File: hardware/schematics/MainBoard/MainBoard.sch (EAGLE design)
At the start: 17 parts

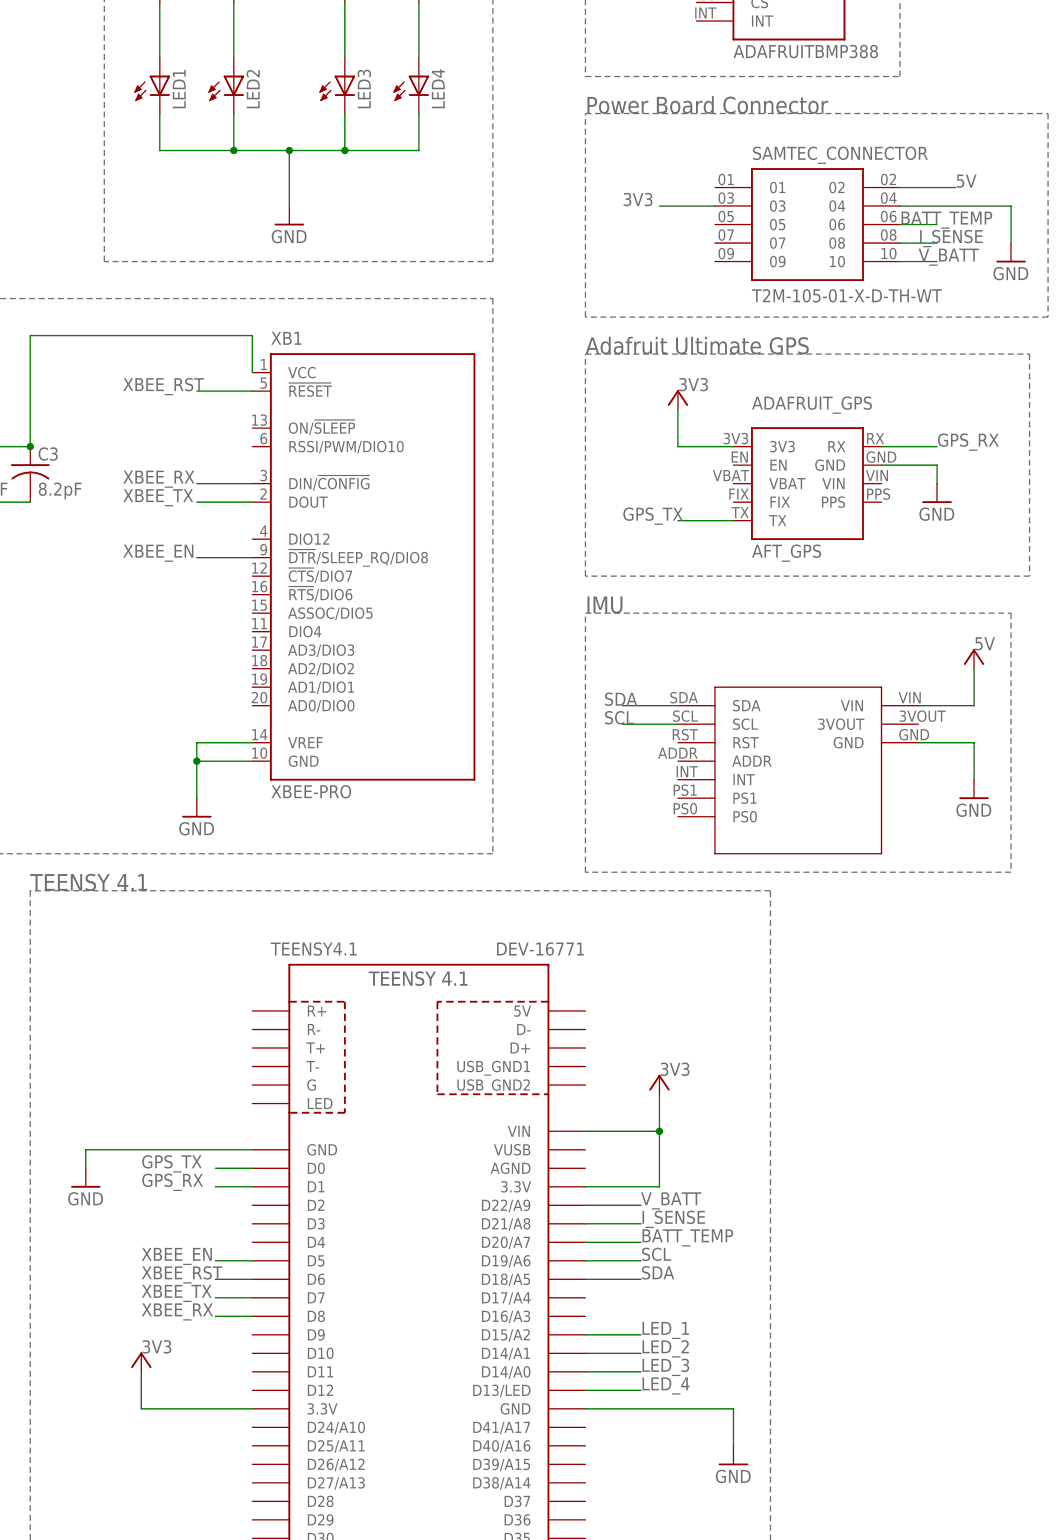
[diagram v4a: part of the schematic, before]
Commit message: MainBoard Power routing & Power Board PNG
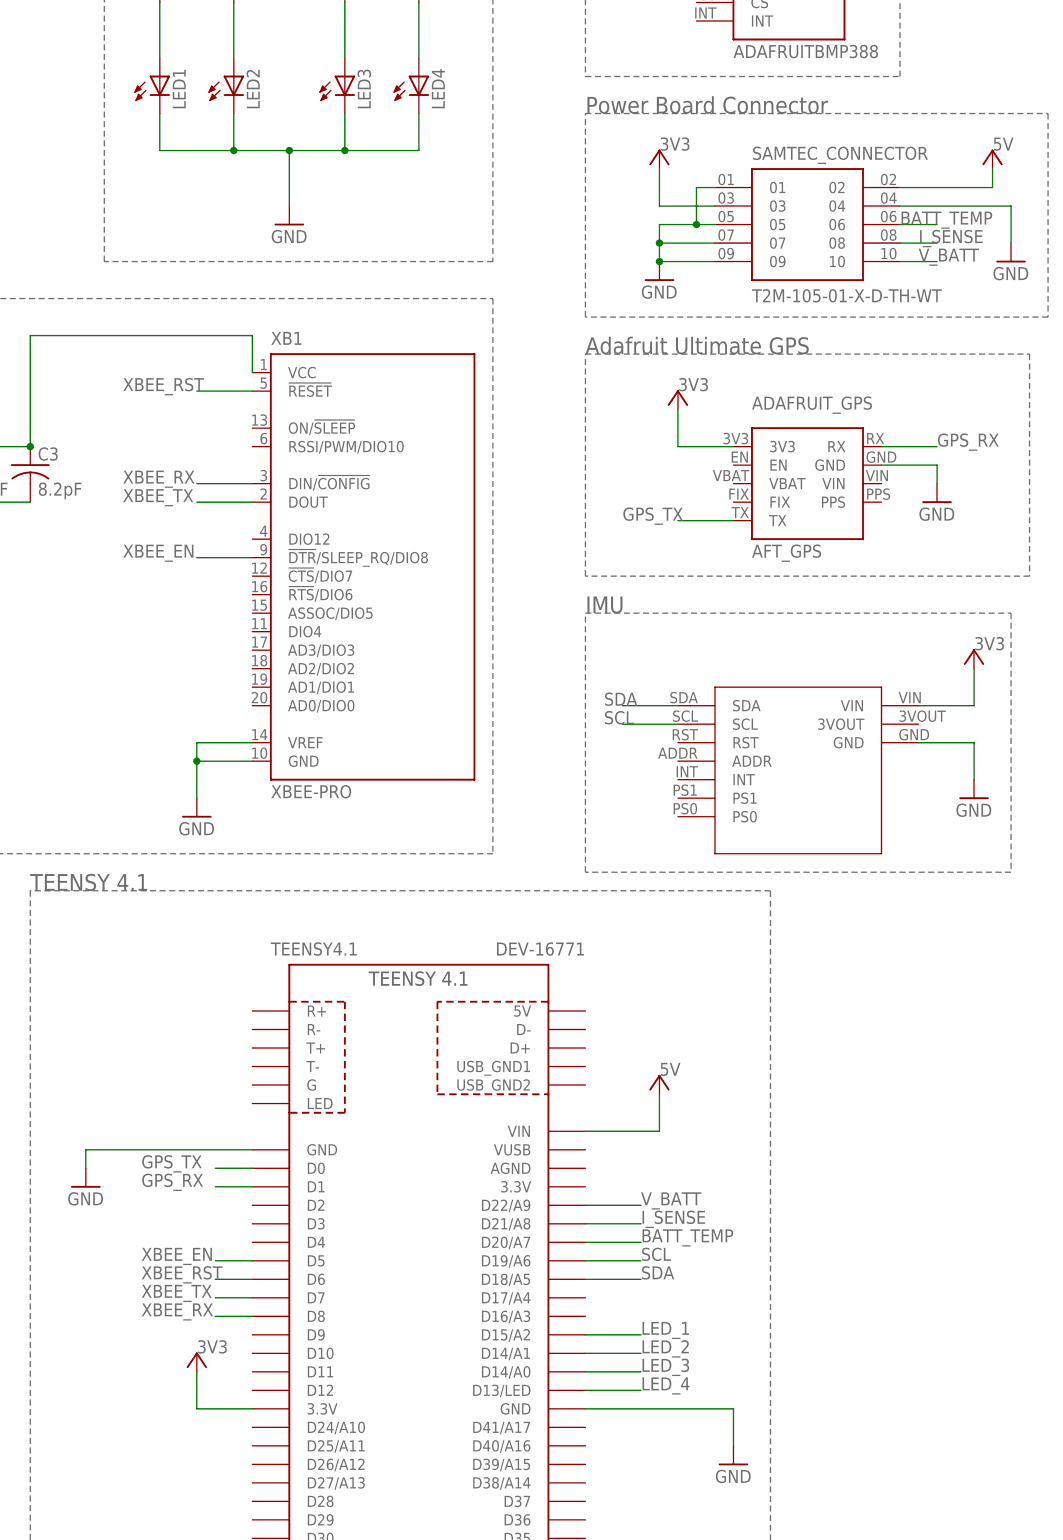
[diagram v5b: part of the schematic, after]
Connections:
- net 3V3: now also U$1.VIN; no longer TEENSY4.1.3.3V@1, TEENSY4.1.VIN
- net 5V: now also TEENSY4.1.VIN; no longer U$1.VIN
- net GND: now also SAMTEC_CONNECTOR.01, SAMTEC_CONNECTOR.05, SAMTEC_CONNECTOR.07, SAMTEC_CONNECTOR.09
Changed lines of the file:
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@@
 <part name="P+4" library="supply1" library_urn="urn:adsk.eagle:library:371" deviceset="VCC" device=""/>
 <part name="GND4" library="supply1" library_urn="urn:adsk.eagle:library:371" deviceset="GND" device=""/>
+<part name="ADAFRUIT_BMP388" library="adafruit BMP388" deviceset="ADAFRUITBMP388" device=""/>
+<part name="GND9" library="supply1" library_urn="urn:adsk.eagle:library:371" deviceset="GND" device=""/>
+<part name="P+6" library="supply1" library_urn="urn:adsk.eagle:library:371" deviceset="VCC" device=""/>
+<part name="P+7" library="supply1" library_urn="urn:adsk.eagle:library:371" deviceset="VCC" device=""/>
 <part name="P+5" library="supply1" library_urn="urn:adsk.eagle:library:371" deviceset="VCC" device=""/>
-<part name="ADAFRUIT_BMP388" library="adafruit BMP388" deviceset="ADAFRUITBMP388" device=""/>
 </parts>
 <sheets>
@@
 <attribute name="VALUE" x="124.46" y="-48.26" size="1.778" layer="96"/>
 </instance>
-<instance part="P+5" gate="VCC" x="12.7" y="-121.92" smashed="yes"/>
 <instance part="ADAFRUIT_BMP388" gate="G$1" x="101.6" y="68.58" smashed="yes">
 <attribute name="VALUE" x="93.98" y="55.88" size="1.778" layer="96"/>
 <attribute name="NAME" x="93.98" y="81.28" size="1.778" layer="95"/>
 </instance>
+<instance part="GND9" gate="1" x="83.82" y="25.4" smashed="yes">
+<attribute name="VALUE" x="81.28" y="22.86" size="1.778" layer="96"/>
+</instance>
+<instance part="P+6" gate="VCC" x="83.82" y="43.18" smashed="yes"/>
+<instance part="P+7" gate="VCC" x="129.54" y="43.18" smashed="yes"/>
+<instance part="P+5" gate="VCC" x="20.32" y="-121.92" smashed="yes"/>
 </instances>
 <busses>
@@
 </segment>
 <segment>
-<pinref part="TEENSY4.1" gate="G$1" pin="VIN"/>
-<wire x1="73.66" y1="-91.44" x2="83.82" y2="-91.44" width="0.1524" layer="91"/>
-<wire x1="83.82" y1="-91.44" x2="83.82" y2="-86.36" width="0.1524" layer="91"/>
-<pinref part="P+3" gate="VCC" pin="VCC"/>
-<label x="83.82" y="-83.82" size="1.778" layer="95"/>
-<pinref part="TEENSY4.1" gate="G$1" pin="3.3V@1"/>
-<wire x1="73.66" y1="-99.06" x2="83.82" y2="-99.06" width="0.1524" layer="91"/>
-<wire x1="83.82" y1="-99.06" x2="83.82" y2="-91.44" width="0.1524" layer="91"/>
-<junction x="83.82" y="-91.44"/>
-</segment>
-<segment>
-<pinref part="SAMTEC_CONNECTOR" gate="G$1" pin="03"/>
-<wire x1="91.44" y1="35.56" x2="83.82" y2="35.56" width="0.1524" layer="91"/>
-<label x="78.74" y="35.56" size="1.778" layer="95"/>
-</segment>
-<segment>
-<pinref part="TEENSY4.1" gate="G$1" pin="3.3V"/>
-<wire x1="27.94" y1="-129.54" x2="12.7" y2="-129.54" width="0.1524" layer="91"/>
-<wire x1="12.7" y1="-129.54" x2="12.7" y2="-124.46" width="0.1524" layer="91"/>
-<pinref part="P+5" gate="VCC" pin="VCC"/>
-<label x="12.7" y="-121.92" size="1.778" layer="95"/>
-</segment>
-<segment>
 <pinref part="ADAFRUIT_BMP388" gate="G$1" pin="VIN"/>
 <wire x1="88.9" y1="78.74" x2="83.82" y2="78.74" width="0.1524" layer="91"/>
 <label x="81.28" y="78.74" size="1.778" layer="95"/>
+</segment>
+<segment>
+<pinref part="SAMTEC_CONNECTOR" gate="G$1" pin="03"/>
+<wire x1="91.44" y1="35.56" x2="83.82" y2="35.56" width="0.1524" layer="91"/>
+<label x="83.82" y="43.18" size="1.778" layer="95"/>
+<pinref part="P+6" gate="VCC" pin="VCC"/>
+<wire x1="83.82" y1="35.56" x2="83.82" y2="40.64" width="0.1524" layer="91"/>
+</segment>
+<segment>
+<pinref part="U$1" gate="G$1" pin="VIN"/>
+<wire x1="119.38" y1="-33.02" x2="127" y2="-33.02" width="0.1524" layer="91"/>
+<wire x1="127" y1="-33.02" x2="127" y2="-27.94" width="0.1524" layer="91"/>
+<pinref part="P+4" gate="VCC" pin="VCC"/>
+<label x="127" y="-25.4" size="1.778" layer="95"/>
+</segment>
+<segment>
+<pinref part="TEENSY4.1" gate="G$1" pin="3.3V"/>
+<wire x1="27.94" y1="-129.54" x2="20.32" y2="-129.54" width="0.1524" layer="91"/>
+<wire x1="20.32" y1="-129.54" x2="20.32" y2="-124.46" width="0.1524" layer="91"/>
+<pinref part="P+5" gate="VCC" pin="VCC"/>
+<label x="20.32" y="-121.92" size="1.778" layer="95"/>
 </segment>
 </net>
@@
 <label x="81.28" y="73.66" size="1.778" layer="95"/>
 </segment>
+<segment>
+<pinref part="SAMTEC_CONNECTOR" gate="G$1" pin="05"/>
+<wire x1="91.44" y1="33.02" x2="88.9" y2="33.02" width="0.1524" layer="91"/>
+<wire x1="88.9" y1="33.02" x2="83.82" y2="33.02" width="0.1524" layer="91"/>
+<wire x1="83.82" y1="33.02" x2="83.82" y2="30.48" width="0.1524" layer="91"/>
+<pinref part="GND9" gate="1" pin="GND"/>
+<pinref part="SAMTEC_CONNECTOR" gate="G$1" pin="09"/>
+<wire x1="83.82" y1="30.48" x2="83.82" y2="27.94" width="0.1524" layer="91"/>
+<wire x1="91.44" y1="27.94" x2="83.82" y2="27.94" width="0.1524" layer="91"/>
+<junction x="83.82" y="27.94"/>
+<pinref part="SAMTEC_CONNECTOR" gate="G$1" pin="07"/>
+<wire x1="91.44" y1="30.48" x2="83.82" y2="30.48" width="0.1524" layer="91"/>
+<junction x="83.82" y="30.48"/>
+<pinref part="SAMTEC_CONNECTOR" gate="G$1" pin="01"/>
+<wire x1="91.44" y1="38.1" x2="88.9" y2="38.1" width="0.1524" layer="91"/>
+<wire x1="88.9" y1="38.1" x2="88.9" y2="33.02" width="0.1524" layer="91"/>
+<junction x="88.9" y="33.02"/>
+</segment>
 </net>
 <net name="XBEE_TX" class="0">
@@
 <segment>
 <pinref part="SAMTEC_CONNECTOR" gate="G$1" pin="02"/>
-<wire x1="116.84" y1="38.1" x2="124.46" y2="38.1" width="0.1524" layer="91"/>
-<label x="124.46" y="38.1" size="1.778" layer="95"/>
-</segment>
-<segment>
-<pinref part="U$1" gate="G$1" pin="VIN"/>
-<wire x1="119.38" y1="-33.02" x2="127" y2="-33.02" width="0.1524" layer="91"/>
-<wire x1="127" y1="-33.02" x2="127" y2="-27.94" width="0.1524" layer="91"/>
-<pinref part="P+4" gate="VCC" pin="VCC"/>
-<label x="127" y="-25.4" size="1.778" layer="95"/>
-</segment>
-</net>
+<wire x1="116.84" y1="38.1" x2="129.54" y2="38.1" width="0.1524" layer="91"/>
+<pinref part="P+7" gate="VCC" pin="VCC"/>
+<wire x1="129.54" y1="38.1" x2="129.54" y2="40.64" width="0.1524" layer="91"/>
+<label x="129.54" y="43.18" size="1.778" layer="95"/>
+</segment>
+<segment>
+<pinref part="TEENSY4.1" gate="G$1" pin="VIN"/>
+<wire x1="73.66" y1="-91.44" x2="83.82" y2="-91.44" width="0.1524" layer="91"/>
+<wire x1="83.82" y1="-91.44" x2="83.82" y2="-86.36" width="0.1524" layer="91"/>
+<pinref part="P+3" gate="VCC" pin="VCC"/>
+<label x="83.82" y="-83.82" size="1.778" layer="95"/>
+</segment>
+</net>
